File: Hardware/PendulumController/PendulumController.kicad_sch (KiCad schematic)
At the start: 11 parts, among them J101 MOTOR, J102 ENCODER

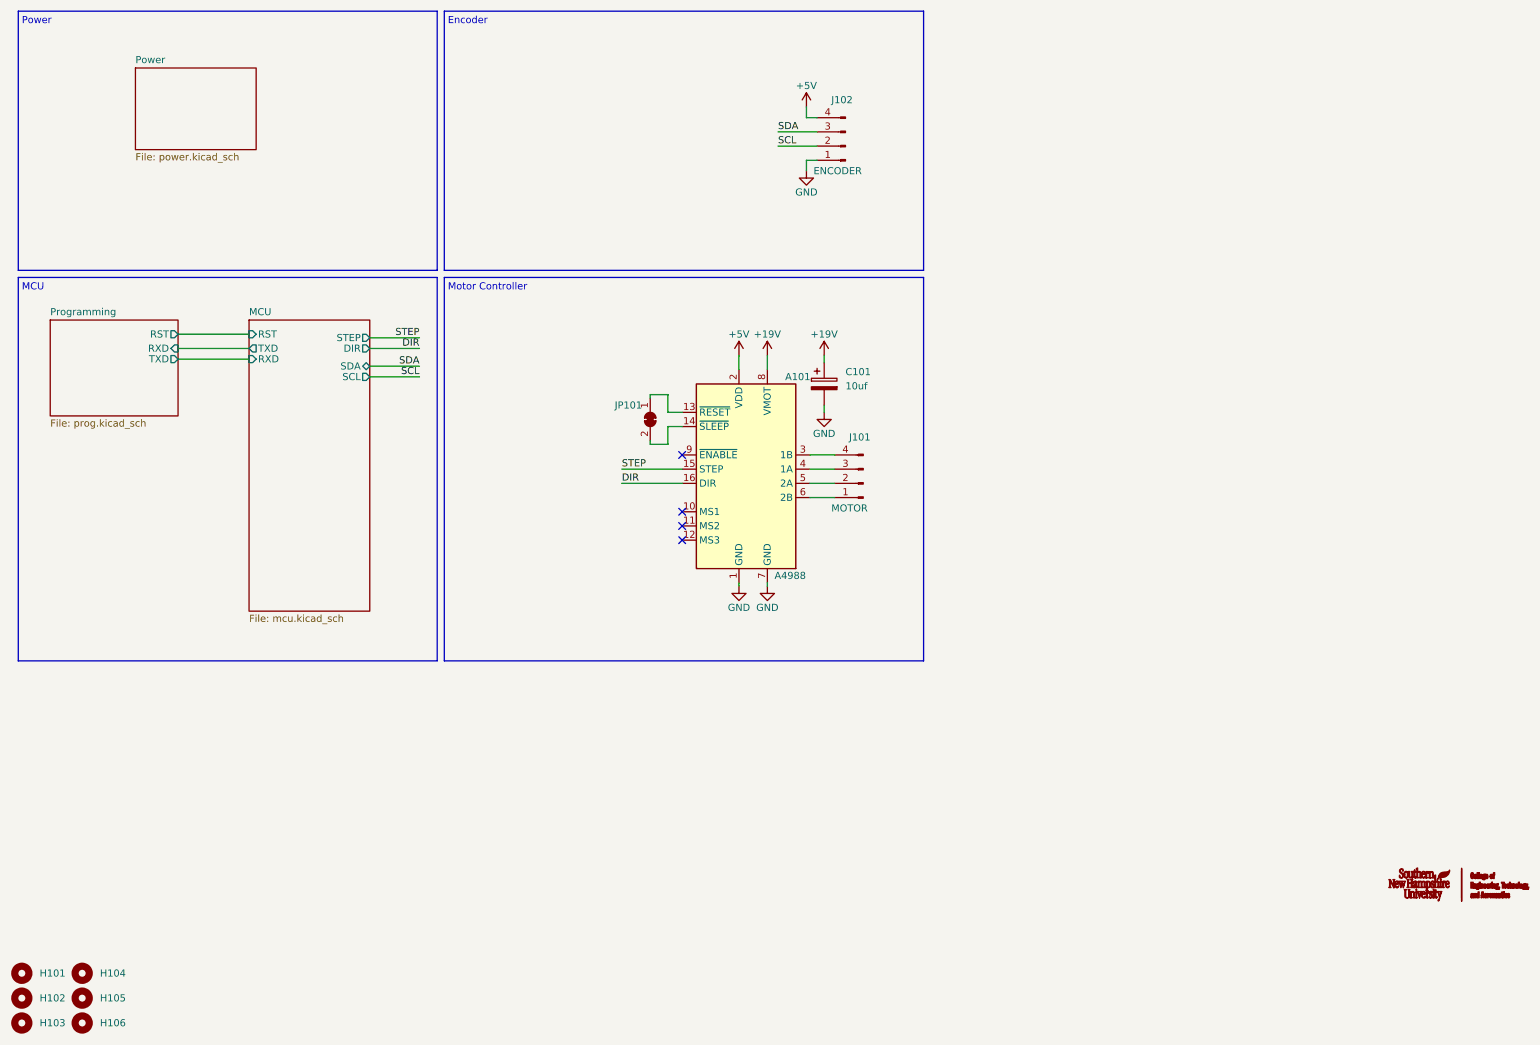
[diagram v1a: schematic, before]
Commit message: Add TFT connector
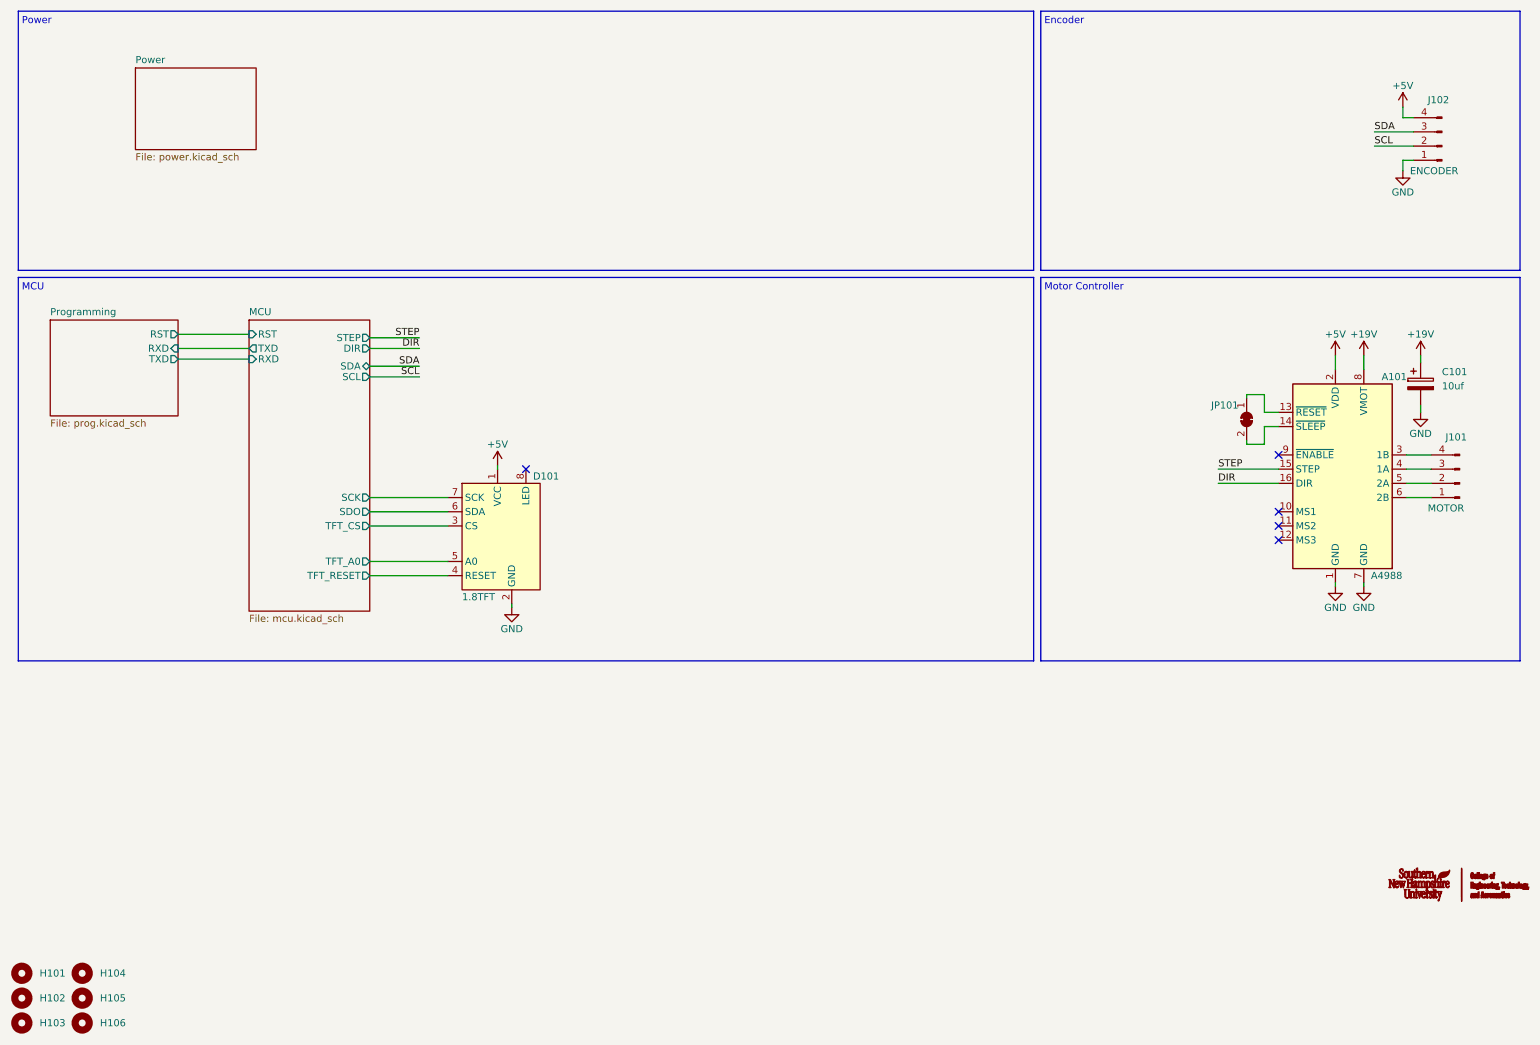
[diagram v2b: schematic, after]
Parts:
- added D101: 1.8TFT, Connector_JST:JST_EH_B8B-EH-A_1x08_P2.50mm_Vertical, symbol KenwoodFox:1.8TFT
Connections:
- net +5V: now also D101.1 (VCC)
- net GND: now also D101.2 (GND)
- new net MCU/SCK: D101.7 (SCK)
- new net MCU/SDO: D101.6 (SDA)
- new net MCU/TFT_A0: D101.5 (A0)
- new net MCU/TFT_CS: D101.3 (CS)
- new net MCU/TFT_RESET: D101.4 (RESET)
- no-connect marks 4 -> 5
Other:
- sheet MCU ports: added SCK, SDO, TFT_A0, TFT_CS, TFT_RESET; removed none
- moved on the sheet: A101, C101, J101, J102, JP101

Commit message: V1 Board (#3)
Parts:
- removed D101: 1.8TFT, Connector_JST:JST_EH_B8B-EH-A_1x08_P2.50mm_Vertical, symbol KenwoodFox:1.8TFT
- removed J102: ENCODER, Connector_JST:JST_EH_B4B-EH-A_1x04_P2.50mm_Vertical, symbol Connector:Conn_01x04_Male
- added C102: EYE_SP, Connector_FFC-FPC:Hirose_FH12-18S-0.5SH_1x18-1MP_P0.50mm_Horizontal, symbol KenwoodFox:EYE_SP
- added J102: ENCODER, Connector_JST:JST_EH_B5B-EH-A_1x05_P2.50mm_Vertical, symbol Connector:Conn_01x05_Male
- added Q101: MMBT3904, Package_TO_SOT_SMD:SOT-23, symbol Transistor_BJT:MMBT3904
- added Q102: MMBT3906, Package_TO_SOT_SMD:SOT-23, symbol Transistor_BJT:MMBT3906
- added R101: 10K, Resistor_SMD:R_0805_2012Metric, symbol Device:R_Small
- added R102: TBD, Resistor_SMD:R_0805_2012Metric, symbol Device:R_Small
- added TP101, TP102: TestPoint, TestPoint:TestPoint_Pad_1.5x1.5mm, symbol Connector:TestPoint
- added TP103, TP104, TP105, TP106, TP107, TP108: TestPoint, TestPoint:TestPoint_Pad_1.0x1.0mm, symbol Connector:TestPoint
- C101: value 10uf -> 470uF
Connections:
- net +5V: now also C102.18 (VCC), J102.5 (Pin_5), Q102.2 (E)
- net GND: now also C102.16 (GND), J102.1 (Pin_1), J102.2 (Pin_2), Q101.2 (E)
- net EN: now reaches A101.9 (~{ENABLE})
- net EN: now also R101.1
- new net: Q101.1 (B), R101.2
- new net: Q101.3 (C), R102.1
- new net: Q102.1 (B), R102.2
- new net DATA/COMMAND: C102.12 (D/C), TP106.1
- new net EncA: J102.3 (Pin_3), TP102.1
- new net EncB: J102.4 (Pin_4), TP101.1
- new net RESET: C102.11 (RESET), TP107.1
- new net SCK: C102.15 (SCK), TP103.1
- new net SDI: C102.14 (SDO), TP104.1
- new net SDO: C102.13 (SDI), TP105.1
- new net SD_CS: C102.9 (SD_CS)
- new net TFT_CS: C102.10 (DISP_CS), TP108.1
- new net TFT_LED: C102.17 (BackLite), Q102.3 (C)
- no-connect marks 5 -> 11
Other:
- sheet MCU ports: added EN, EncA, EncB, SDI, SD_CS, TFT_DC; removed SCL, SDA, TFT_A0
- note added: "BAC (Big Ass Capacitor)"
- note added: "Black"
- note added: "Circuit to switch the TFT backlight on and off with the ENABLE/SLEEP signal."
- note added: "Phase A"
- note added: "Phase B"
- note added: "Shield"
- note added: "VCC"
- moved on the sheet: C101

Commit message: Firmware (#15)
Merged for PRR
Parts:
- added R103, R104, R105: 50R, Resistor_SMD:R_0805_2012Metric, symbol Device:R_Small
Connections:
- net SCK: now also R103.2; no longer C102.15 (SCK)
- net SDI: now also R105.2; no longer C102.14 (SDO)
- net SDO: now also R104.2; no longer C102.13 (SDI)
- new net: C102.15 (SCK), R103.1
- new net: C102.13 (SDI), R104.1
- new net: C102.14 (SDO), R105.1
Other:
- moved on the sheet: C102
